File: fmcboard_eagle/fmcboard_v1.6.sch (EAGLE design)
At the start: 284 parts, among them IC1 OPA699ID, IC10 LM358, IC11 7805DT, IC12 SN74AUC2G66DCTR, IC13 SN74AUC2G66DCTR, IC14 SN74AUC2G66DCTR, IC15 SN74AUC2G66DCTR, IC16 DAC7578SPWR, IC17 SN74AUC2G66DCTR, IC18 SN74AUC2G66DCTR, IC19 SN74AUC2G66DCTR, IC2 DAC7578SPWR, IC20 SN74AUC2G66DCTR, IC21 74AUP2GU04GW, IC22 74AUP2GU04GW, IC23 74AUP2GU04GW, IC24 74AUP2GU04GW, IC25 MC7905ACD2TR4G, IC26 AMS1117-1.8, IC27 LM358, IC28 SN74AUC2G66DCTR, IC29 LM337KVURG3, IC3 LTC6229IMS8E#TRPBF, IC30 SN74AUC2G66DCTR, IC31 SN74AUC2G66DCTR, IC32 SN74AUC2G66DCTR, IC33 LTC6229IMS8E#TRPBF, IC34 74AUP2GU04GW, IC35 74AUP2GU04GW, IC4 OPA695IDR, IC5 LTC6229IMS8E#TRPBF, IC6 OPA695IDR, IC7 OPA699ID, IC8 LM358, IC9 LM358, J1 8pin, J12 4p-2.54, J13 4p-2.54, J2 ASP-134604-01, J3 4p-2.54, J4 4p-2.54, J5 4p-2.54, J6 4p-2.54, J7 4p-2.54, J8 4p-2.54

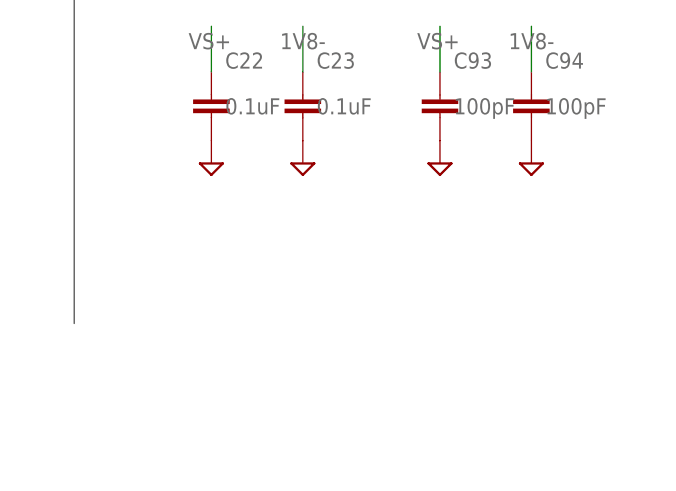
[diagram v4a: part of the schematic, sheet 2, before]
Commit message: Added extra 4 DAC outputs, 2 positive and 2 negative Move all to 0402 R and C Replace 100uF with 10 10uF Remove dacoffset variable resistor, replace with DAC N Set VH and VL to 1.8 and GND Copies of pulse out and amp out to sma - nah
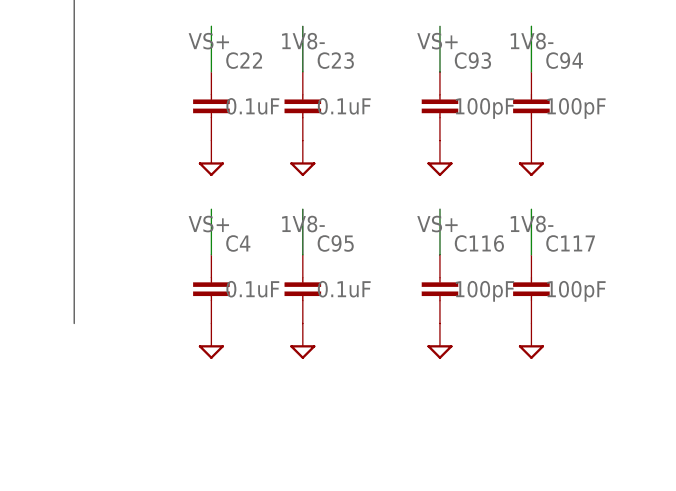
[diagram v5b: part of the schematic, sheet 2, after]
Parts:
- removed C8: 0.1uF, rcl:C-EUC0402K
- added C116, C117: 100pF, rcl:C-EUC0402K
- added C4, C95: 0.1uF, rcl:C-EUC0402K
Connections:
- net 1V8-: now also C117.1, C95.1
- net GND: now also C116.2, C117.2, C4.2, C95.2; no longer C8.1, C8.2
- net VS+: now also C116.1, C4.1
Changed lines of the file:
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@@
 <part name="C5" library="rcl" library_urn="urn:adsk.eagle:library:334" deviceset="C-EU" device="C0402K" package3d_urn="urn:adsk.eagle:package:23679/2" value="0.1uF"/>
 <part name="C7" library="rcl" library_urn="urn:adsk.eagle:library:334" deviceset="C-EU" device="C0402K" package3d_urn="urn:adsk.eagle:package:23679/2" value="0.1uF"/>
-<part name="C8" library="rcl" library_urn="urn:adsk.eagle:library:334" deviceset="C-EU" device="C0402K" package3d_urn="urn:adsk.eagle:package:23679/2" value="0.1uF"/>
 <part name="C9" library="rcl" library_urn="urn:adsk.eagle:library:334" deviceset="C-EU" device="C0402K" package3d_urn="urn:adsk.eagle:package:23679/2" value="0.1uF"/>
 <part name="C10" library="rcl" library_urn="urn:adsk.eagle:library:334" deviceset="C-EU" device="C0402K" package3d_urn="urn:adsk.eagle:package:23679/2" value="0.1uF"/>
@@
 <part name="C14" library="rcl" library_urn="urn:adsk.eagle:library:334" deviceset="C-EU" device="C0402K" package3d_urn="urn:adsk.eagle:package:23679/2" value="0.1uF"/>
 <part name="SUPPLY9" library="supply2" library_urn="urn:adsk.eagle:library:372" deviceset="GND" device=""/>
-<part name="SUPPLY10" library="supply2" library_urn="urn:adsk.eagle:library:372" deviceset="GND" device=""/>
 <part name="SUPPLY11" library="supply2" library_urn="urn:adsk.eagle:library:372" deviceset="GND" device=""/>
 <part name="SUPPLY12" library="supply2" library_urn="urn:adsk.eagle:library:372" deviceset="GND" device=""/>
@@
 <part name="R115" library="rcl" library_urn="urn:adsk.eagle:library:334" deviceset="R-US_" device="R0402" package3d_urn="urn:adsk.eagle:package:23547/3" value="1k"/>
 <part name="SUPPLY6" library="supply2" library_urn="urn:adsk.eagle:library:372" deviceset="GND" device=""/>
+<part name="C4" library="rcl" library_urn="urn:adsk.eagle:library:334" deviceset="C-EU" device="C0402K" package3d_urn="urn:adsk.eagle:package:23679/2" value="0.1uF"/>
+<part name="C95" library="rcl" library_urn="urn:adsk.eagle:library:334" deviceset="C-EU" device="C0402K" package3d_urn="urn:adsk.eagle:package:23679/2" value="0.1uF"/>
+<part name="SUPPLY22" library="supply2" library_urn="urn:adsk.eagle:library:372" deviceset="GND" device=""/>
+<part name="SUPPLY23" library="supply2" library_urn="urn:adsk.eagle:library:372" deviceset="GND" device=""/>
+<part name="C116" library="rcl" library_urn="urn:adsk.eagle:library:334" deviceset="C-EU" device="C0402K" package3d_urn="urn:adsk.eagle:package:23679/2" value="100pF"/>
+<part name="C117" library="rcl" library_urn="urn:adsk.eagle:library:334" deviceset="C-EU" device="C0402K" package3d_urn="urn:adsk.eagle:package:23679/2" value="100pF"/>
+<part name="SUPPLY144" library="supply2" library_urn="urn:adsk.eagle:library:372" deviceset="GND" device=""/>
+<part name="SUPPLY145" library="supply2" library_urn="urn:adsk.eagle:library:372" deviceset="GND" device=""/>
 </parts>
 <sheets>
@@
 <attribute name="VALUE" x="98.044" y="28.321" size="1.778" layer="96"/>
 </instance>
-<instance part="C8" gate="G$1" x="106.68" y="30.48" smashed="yes">
-<attribute name="NAME" x="108.204" y="33.401" size="1.778" layer="95"/>
-<attribute name="VALUE" x="108.204" y="28.321" size="1.778" layer="96"/>
-</instance>
 <instance part="C9" gate="G$1" x="76.2" y="30.48" smashed="yes">
 <attribute name="NAME" x="77.724" y="33.401" size="1.778" layer="95"/>
@@
 </instance>
 <instance part="SUPPLY9" gate="GND" x="96.52" y="22.86" smashed="yes"/>
-<instance part="SUPPLY10" gate="GND" x="106.68" y="22.86" smashed="yes"/>
 <instance part="SUPPLY11" gate="GND" x="76.2" y="22.86" smashed="yes"/>
 <instance part="SUPPLY12" gate="GND" x="86.36" y="22.86" smashed="yes"/>
@@
 </segment>
 <segment>
-<pinref part="C8" gate="G$1" pin="2"/>
-<pinref part="SUPPLY10" gate="GND" pin="GND"/>
-</segment>
-<segment>
 <pinref part="C9" gate="G$1" pin="2"/>
 <pinref part="SUPPLY11" gate="GND" pin="GND"/>
@@
 <label x="121.92" y="33.02" size="1.778" layer="95"/>
 </segment>
-<segment>
-<pinref part="C8" gate="G$1" pin="1"/>
-<wire x1="106.68" y1="33.02" x2="106.68" y2="40.64" width="0.1524" layer="91"/>
-<label x="104.14" y="38.1" size="1.778" layer="95"/>
-</segment>
 </net>
 <net name="1V8" class="1">
@@
 </instance>
 <instance part="SUPPLY143" gate="GND" x="-68.58" y="-40.64" smashed="yes"/>
+<instance part="C4" gate="G$1" x="251.46" y="-22.86" smashed="yes">
+<attribute name="NAME" x="252.984" y="-19.939" size="1.778" layer="95"/>
+<attribute name="VALUE" x="252.984" y="-25.019" size="1.778" layer="96"/>
+</instance>
+<instance part="C95" gate="G$1" x="261.62" y="-22.86" smashed="yes">
+<attribute name="NAME" x="263.144" y="-19.939" size="1.778" layer="95"/>
+<attribute name="VALUE" x="263.144" y="-25.019" size="1.778" layer="96"/>
+</instance>
+<instance part="SUPPLY22" gate="GND" x="251.46" y="-30.48" smashed="yes"/>
+<instance part="SUPPLY23" gate="GND" x="261.62" y="-30.48" smashed="yes"/>
+<instance part="C116" gate="G$1" x="276.86" y="-22.86" smashed="yes">
+<attribute name="NAME" x="278.384" y="-19.939" size="1.778" layer="95"/>
+<attribute name="VALUE" x="278.384" y="-25.019" size="1.778" layer="96"/>
+</instance>
+<instance part="C117" gate="G$1" x="287.02" y="-22.86" smashed="yes">
+<attribute name="NAME" x="288.544" y="-19.939" size="1.778" layer="95"/>
+<attribute name="VALUE" x="288.544" y="-25.019" size="1.778" layer="96"/>
+</instance>
+<instance part="SUPPLY144" gate="GND" x="276.86" y="-30.48" smashed="yes"/>
+<instance part="SUPPLY145" gate="GND" x="287.02" y="-30.48" smashed="yes"/>
 </instances>
 <busses>
@@
 <label x="-50.8" y="-38.1" size="1.778" layer="95"/>
 </segment>
+<segment>
+<pinref part="C4" gate="G$1" pin="2"/>
+<pinref part="SUPPLY22" gate="GND" pin="GND"/>
+</segment>
+<segment>
+<pinref part="C95" gate="G$1" pin="2"/>
+<pinref part="SUPPLY23" gate="GND" pin="GND"/>
+</segment>
+<segment>
+<pinref part="C116" gate="G$1" pin="2"/>
+<pinref part="SUPPLY144" gate="GND" pin="GND"/>
+</segment>
+<segment>
+<pinref part="C117" gate="G$1" pin="2"/>
+<pinref part="SUPPLY145" gate="GND" pin="GND"/>
+</segment>
 </net>
 <net name="VS+" class="1">
@@
 <pinref part="IC33" gate="G$1" pin="V+"/>
 </segment>
+<segment>
+<pinref part="C4" gate="G$1" pin="1"/>
+<wire x1="251.46" y1="-20.32" x2="251.46" y2="-15.24" width="0.1524" layer="91"/>
+<label x="248.92" y="-17.78" size="1.778" layer="95"/>
+</segment>
+<segment>
+<pinref part="C116" gate="G$1" pin="1"/>
+<wire x1="276.86" y1="-20.32" x2="276.86" y2="-15.24" width="0.1524" layer="91"/>
+<label x="274.32" y="-17.78" size="1.778" layer="95"/>
+</segment>
 </net>
 <net name="VS-" class="1">
@@
 <label x="-63.5" y="-27.94" size="1.778" layer="95"/>
 </segment>
+<segment>
+<pinref part="C95" gate="G$1" pin="1"/>
+<wire x1="261.62" y1="-20.32" x2="261.62" y2="-15.24" width="0.1524" layer="91"/>
+<label x="259.08" y="-17.78" size="1.778" layer="95"/>
+</segment>
+<segment>
+<pinref part="C117" gate="G$1" pin="1"/>
+<wire x1="287.02" y1="-20.32" x2="287.02" y2="-15.24" width="0.1524" layer="91"/>
+<label x="284.48" y="-17.78" size="1.778" layer="95"/>
+</segment>
 </net>

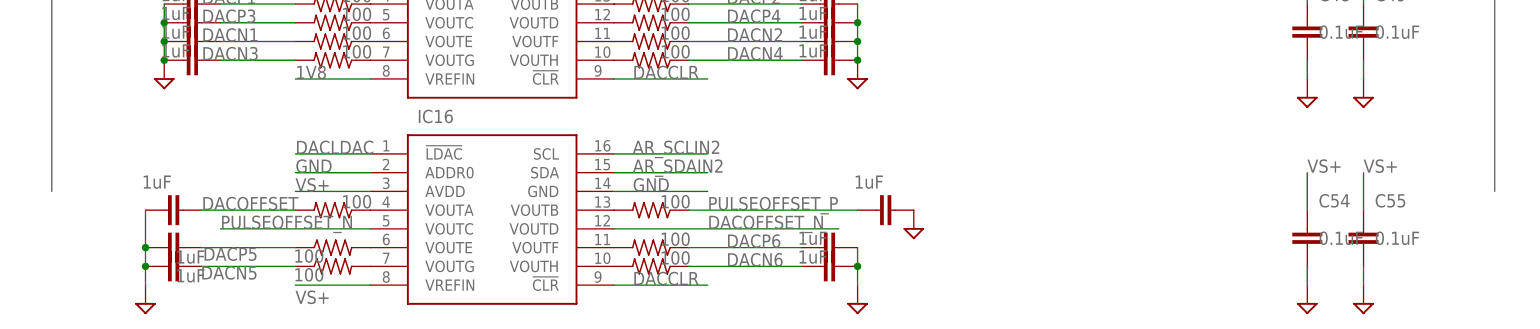
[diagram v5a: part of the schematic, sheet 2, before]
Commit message: power routed
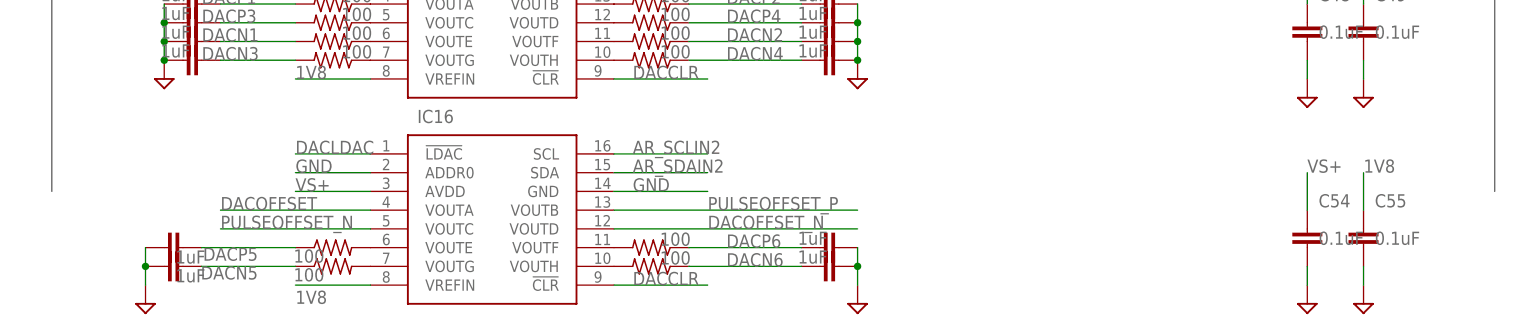
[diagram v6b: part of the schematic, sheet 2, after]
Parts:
- removed C11, C64, C80: 1uF, rcl:C-EUC0402K
- removed R60, R73, R84: 100, rcl:R-US_R0402
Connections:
- removed net N$29: IC16.VOUTA, R60.1
- removed net N$36: IC10G1.OUT, R35.2, R73.2
- removed net N$39: IC16.VOUTB, R84.2
- net 1V8: now also C55.1, IC16.VREFIN
- net DACOFFSET: now also IC16.VOUTA; no longer C64.2, R60.2
- net GND: no longer C11.1, C64.1, C80.2
- net PULSEOFFSET_NI: now also IC10G1.OUT, R35.2; no longer C11.2, R73.1
- net PULSEOFFSET_P: now also IC16.VOUTB; no longer C80.1, R84.1
- net VS+: no longer C55.1, IC16.VREFIN

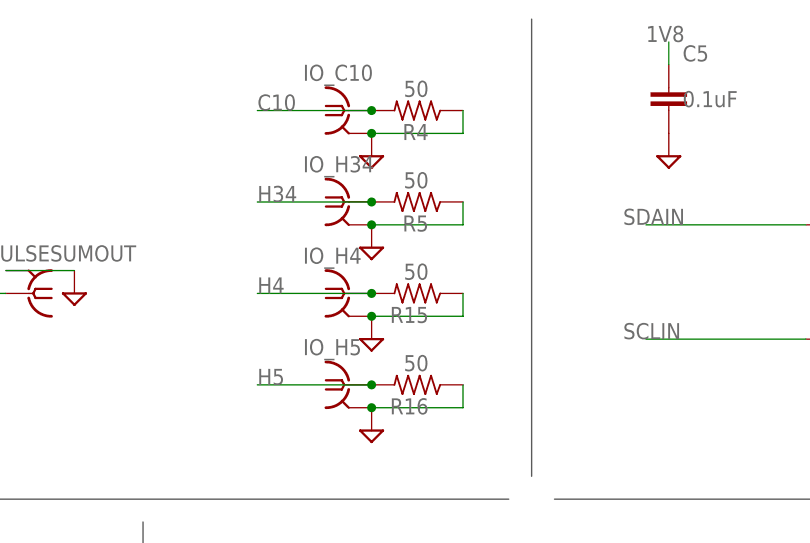
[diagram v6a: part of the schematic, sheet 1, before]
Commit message: power routed
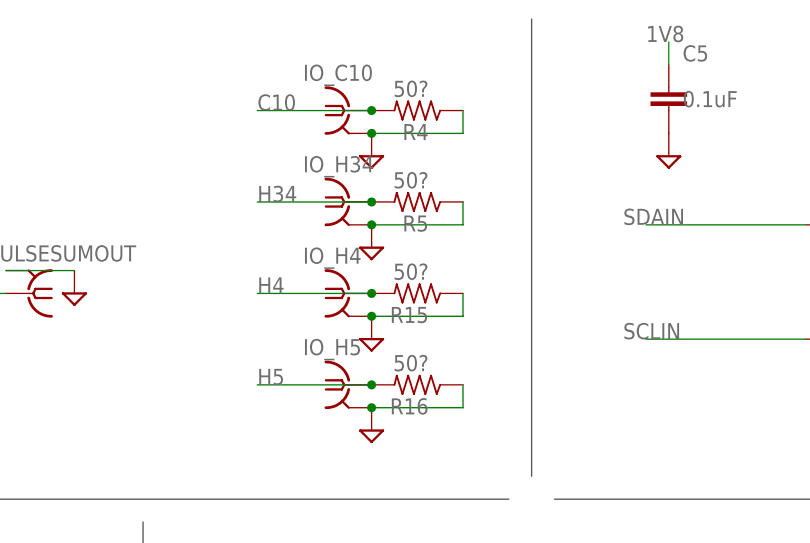
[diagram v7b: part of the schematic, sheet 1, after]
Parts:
- R15, R16, R4, R5: value 50 -> 50?
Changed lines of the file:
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@@
 <part name="SUPPLY27" library="supply2" library_urn="urn:adsk.eagle:library:372" deviceset="GND" device=""/>
 <part name="SUPPLY28" library="supply2" library_urn="urn:adsk.eagle:library:372" deviceset="GND" device=""/>
-<part name="R4" library="rcl" library_urn="urn:adsk.eagle:library:334" deviceset="R-US_" device="R0402" package3d_urn="urn:adsk.eagle:package:23547/3" value="50"/>
-<part name="R5" library="rcl" library_urn="urn:adsk.eagle:library:334" deviceset="R-US_" device="R0402" package3d_urn="urn:adsk.eagle:package:23547/3" value="50"/>
-<part name="R15" library="rcl" library_urn="urn:adsk.eagle:library:334" deviceset="R-US_" device="R0402" package3d_urn="urn:adsk.eagle:package:23547/3" value="50"/>
-<part name="R16" library="rcl" library_urn="urn:adsk.eagle:library:334" deviceset="R-US_" device="R0402" package3d_urn="urn:adsk.eagle:package:23547/3" value="50"/>
+<part name="R4" library="rcl" library_urn="urn:adsk.eagle:library:334" deviceset="R-US_" device="R0402" package3d_urn="urn:adsk.eagle:package:23547/3" value="50?"/>
+<part name="R5" library="rcl" library_urn="urn:adsk.eagle:library:334" deviceset="R-US_" device="R0402" package3d_urn="urn:adsk.eagle:package:23547/3" value="50?"/>
+<part name="R15" library="rcl" library_urn="urn:adsk.eagle:library:334" deviceset="R-US_" device="R0402" package3d_urn="urn:adsk.eagle:package:23547/3" value="50?"/>
+<part name="R16" library="rcl" library_urn="urn:adsk.eagle:library:334" deviceset="R-US_" device="R0402" package3d_urn="urn:adsk.eagle:package:23547/3" value="50?"/>
 <part name="IC3" library="LTC6229IMS8E#TRPBF" deviceset="LTC6229IMS8E#TRPBF" device=""/>
 <part name="R11" library="rcl" library_urn="urn:adsk.eagle:library:334" deviceset="R-US_" device="R0402" package3d_urn="urn:adsk.eagle:package:23547/3" value="1k"/>

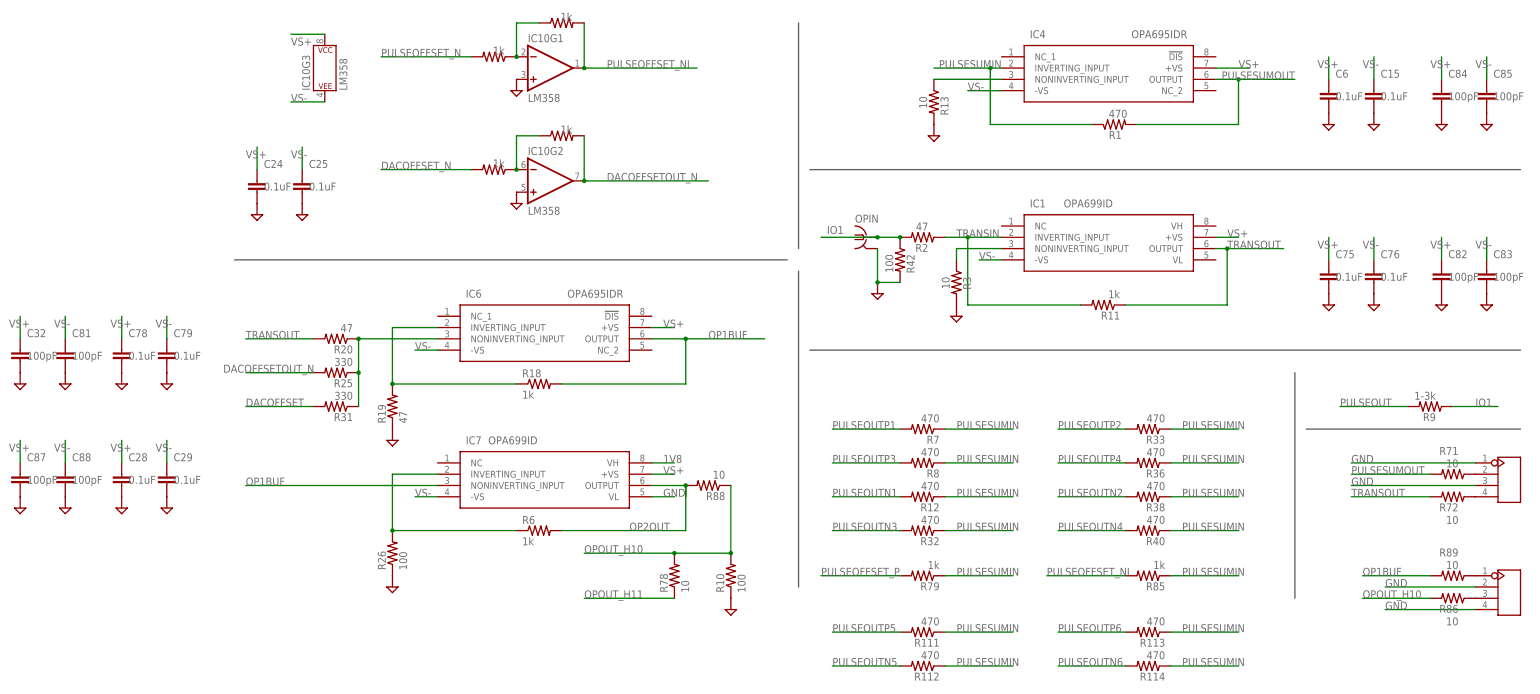
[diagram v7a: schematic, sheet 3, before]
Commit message: cosmetic updates to v1.65
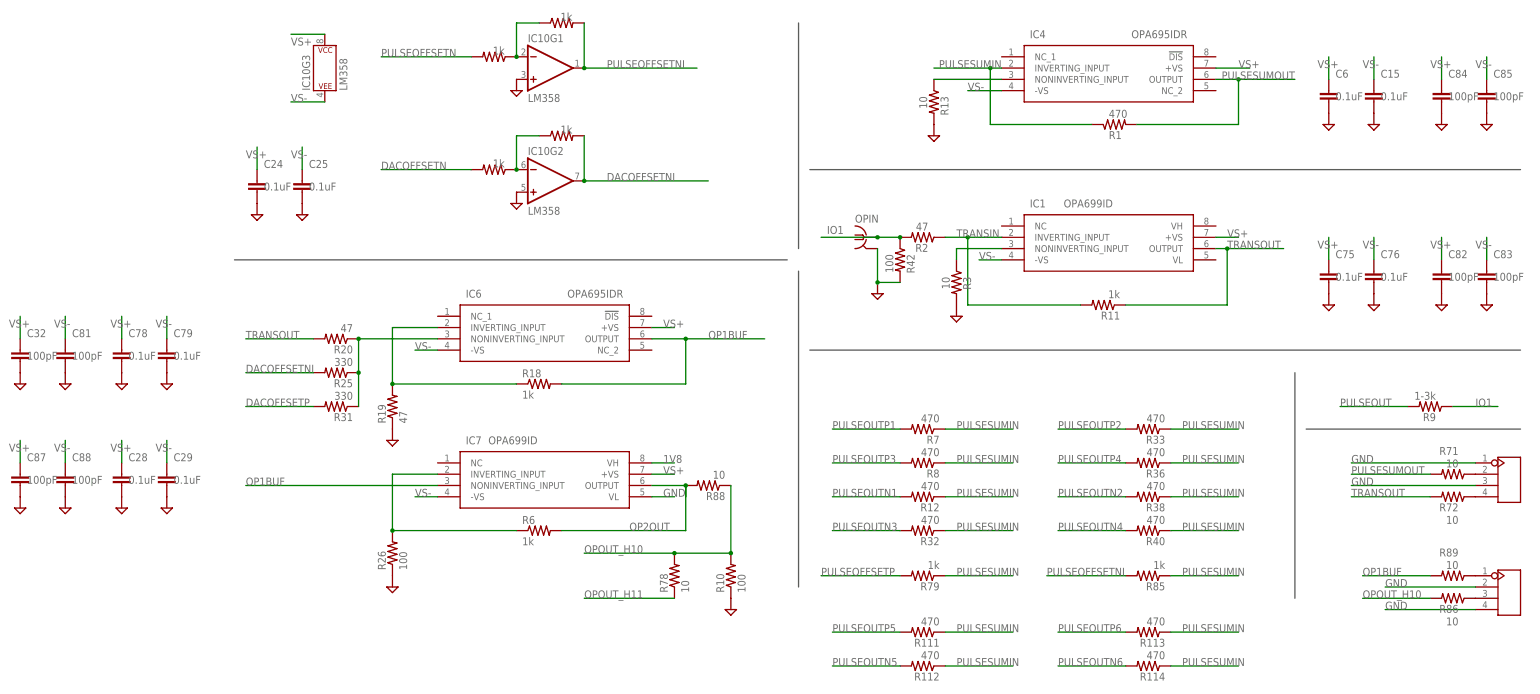
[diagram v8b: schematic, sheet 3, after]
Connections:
- net DACOFFSET renamed DACOFFSETP
- net DACOFFSETOUT_N renamed DACOFFSETNI
- net DACOFFSET_N renamed DACOFFSETN
- net PULSEOFFSET_N renamed PULSEOFFSETN
- net PULSEOFFSET_NI renamed PULSEOFFSETNI
- net PULSEOFFSET_P renamed PULSEOFFSETP
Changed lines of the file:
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@@
 </segment>
 </net>
-<net name="DACOFFSET" class="0">
+<net name="DACOFFSETP" class="0">
 <segment>
 <wire x1="83.82" y1="-30.48" x2="63.5" y2="-30.48" width="0.1524" layer="91"/>
@@
 </segment>
 </net>
-<net name="PULSEOFFSET_P" class="0">
+<net name="PULSEOFFSETP" class="0">
 <segment>
 <wire x1="116.84" y1="-30.48" x2="149.86" y2="-30.48" width="0.1524" layer="91"/>
@@
 </segment>
 </net>
-<net name="PULSEOFFSET_N" class="0">
+<net name="PULSEOFFSETN" class="0">
 <segment>
 <pinref part="IC16" gate="G$1" pin="VOUTC"/>
@@
 </segment>
 </net>
-<net name="DACOFFSET_N" class="0">
+<net name="DACOFFSETN" class="0">
 <segment>
 <pinref part="IC16" gate="G$1" pin="VOUTD"/>
@@
 </segment>
 </net>
-<net name="DACOFFSET" class="0">
+<net name="DACOFFSETP" class="0">
 <segment>
 <pinref part="R31" gate="G$1" pin="2"/>
@@
 </segment>
 </net>
-<net name="PULSEOFFSET_P" class="0">
+<net name="PULSEOFFSETP" class="0">
 <segment>
 <wire x1="134.62" y1="10.16" x2="152.4" y2="10.16" width="0.1524" layer="91"/>
@@
 </segment>
 </net>
-<net name="PULSEOFFSET_NI" class="0">
+<net name="PULSEOFFSETNI" class="0">
 <segment>
 <wire x1="185.42" y1="10.16" x2="203.2" y2="10.16" width="0.1524" layer="91"/>
@@
 </segment>
 </net>
-<net name="PULSEOFFSET_N" class="0">
+<net name="PULSEOFFSETN" class="0">
 <segment>
 <pinref part="R61" gate="G$1" pin="2"/>
@@
 </segment>
 </net>
-<net name="DACOFFSET_N" class="0">
+<net name="DACOFFSETN" class="0">
 <segment>
 <wire x1="55.88" y1="101.6" x2="35.56" y2="101.6" width="0.1524" layer="91"/>
@@
 </segment>
 </net>
-<net name="DACOFFSETOUT_N" class="0">
+<net name="DACOFFSETNI" class="0">
 <segment>
 <pinref part="R115" gate="G$1" pin="2"/>
@@
 <pinref part="R25" gate="G$1" pin="2"/>
 <wire x1="20.32" y1="55.88" x2="5.08" y2="55.88" width="0.1524" layer="91"/>
-<label x="0" y="55.88" size="1.778" layer="95"/>
-</segment>
-</net>
+<label x="5.08" y="55.88" size="1.778" layer="95"/>
+</segment>
+</net>
